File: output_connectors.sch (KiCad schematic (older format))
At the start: 2 parts, among them J2 Frontend Connector

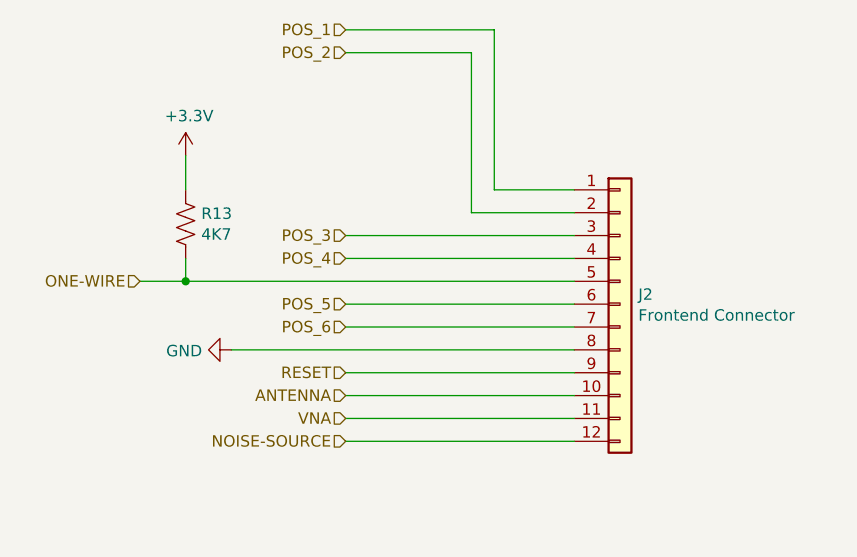
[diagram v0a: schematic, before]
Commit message: Added MFN, MPN, VN and VPN fields for all symbols
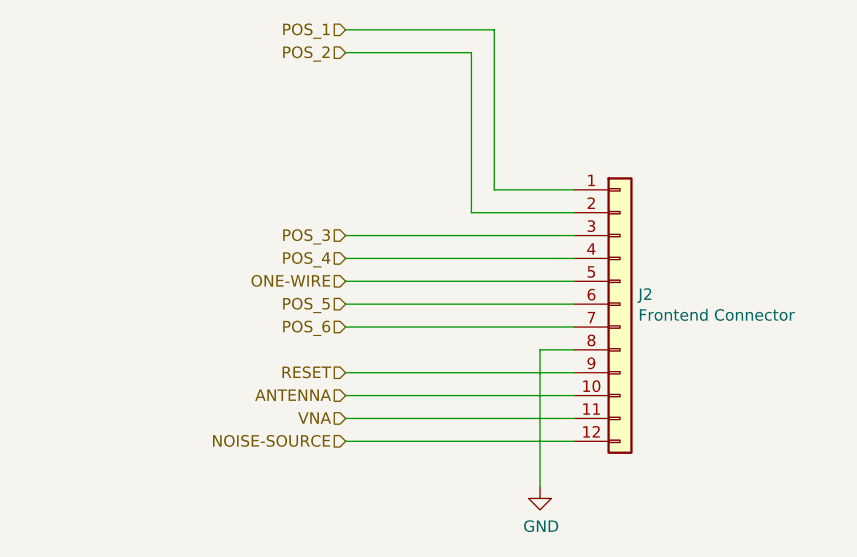
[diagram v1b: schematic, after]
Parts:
- removed R13: 4K7, Resistor_SMD:R_0603_1608Metric_Pad1.05x0.95mm_HandSolder, symbol Device:R_US
- J2: MFN (none) -> CUI Devices; MPN (none) -> TBP02R1-381-12BE; VN (none) -> Digikey; VPN (none) -> 102-6489-ND
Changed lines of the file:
@@
 Comment4 ""
 $EndDescr
-Wire Wire Line
-	4900 3650 4900 3550
-Text HLabel 4700 3650 0    50   Input ~ 0
+Text HLabel 5600 3650 0    50   Input ~ 0
 ONE-WIRE
 Text HLabel 5600 2550 0    50   Input ~ 0
@@
 Wire Wire Line
 	5600 3450 6600 3450
-Wire Wire Line
-	4700 3650 4900 3650
-Connection ~ 4900 3650
-Wire Wire Line
-	4900 3650 6600 3650
-$Comp
-L Device:R_US R?
-U 1 1 5E650E19
-P 4900 3400
-AR Path="/5E650E19" Ref="R?"  Part="1"
-AR Path="/5E64C909/5E650E19" Ref="R13"  Part="1"
-F 0 "R13" H 4968 3446 50  0000 L CNN
-F 1 "4K7" H 4968 3355 50  0000 L CNN
-F 2 "Resistor_SMD:R_0603_1608Metric_Pad1.05x0.95mm_HandSolder" V 4940 3390 50  0001 C CNN
-F 3 "~" H 4900 3400 50  0001 C CNN
-	1    4900 3400
-	1    0    0    -1
-$EndComp
-$Comp
-L power:+3.3V #PWR0151
-U 1 1 5E5353C9
-P 4900 3100
-F 0 "#PWR0151" H 4900 2950 50  0001 C CNN
-F 1 "+3.3V" H 4915 3273 50  0000 C CNN
-F 2 "" H 4900 3100 50  0001 C CNN
-F 3 "" H 4900 3100 50  0001 C CNN
-	1    4900 3100
-	1    0    0    -1
-$EndComp
-Wire Wire Line
-	4900 3100 4900 3250
 Text HLabel 5600 4350 0    50   Input ~ 0
 NOISE-SOURCE
@@
 F 1 "Frontend Connector" H 6880 3701 50  0000 L CNN
 F 2 "Connector_Phoenix_MC:PhoenixContact_MC_1,5_12-G-3.81_1x12_P3.81mm_Horizontal" H 6800 3750 50  0001 C CNN
-F 3 "~" H 6800 3750 50  0001 C CNN
+F 3 "https://www.cuidevices.com/product/resource/tbp02r1-381.pdf" H 6800 3750 50  0001 C CNN
+F 4 "Digikey" H 6800 3750 50  0001 C CNN "VN"
+F 5 "CUI Devices" H 6800 3750 50  0001 C CNN "MFN"
+F 6 "TBP02R1-381-12BE" H 6800 3750 50  0001 C CNN "MPN"
+F 7 "102-6489-ND" H 6800 3750 50  0001 C CNN "VPN"
 	1    6800 3750
 	1    0    0    -1
@@
 Wire Wire Line
 	5600 3750 6600 3750
-Wire Wire Line
-	5100 3950 6600 3950
 Text HLabel 5600 3750 0    50   Input ~ 0
 POS_5
 $Comp
-L power:GND #PWR?
-U 1 1 5E650E31
-P 5100 3950
-AR Path="/5E650E31" Ref="#PWR?"  Part="1"
-AR Path="/5E64C909/5E650E31" Ref="#PWR0152"  Part="1"
-F 0 "#PWR0152" H 5100 3700 50  0001 C CNN
-F 1 "GND" V 5105 3822 50  0000 R CNN
-F 2 "" H 5100 3950 50  0001 C CNN
-F 3 "" H 5100 3950 50  0001 C CNN
-	1    5100 3950
-	0    1    1    0
+L power:GND #PWR0148
+U 1 1 5E62A28F
+P 6450 4550
+F 0 "#PWR0148" H 6450 4300 50  0001 C CNN
+F 1 "GND" H 6455 4377 50  0000 C CNN
+F 2 "" H 6450 4550 50  0001 C CNN
+F 3 "" H 6450 4550 50  0001 C CNN
+	1    6450 4550
+	1    0    0    -1
 $EndComp
+Wire Wire Line
+	6450 4550 6450 3950
+Wire Wire Line
+	6450 3950 6600 3950
+Wire Wire Line
+	6600 3650 5600 3650
 $EndSCHEMATC
